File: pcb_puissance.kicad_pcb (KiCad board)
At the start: 2 copper layers, 133.1 x 126.4 mm, 29 parts, among them J1 1755736, J2 1755736, J3 1755736, J4 1755736, J5 1755736, J6 1755736, J7 1755736, J8 1755736, K1 SRD-05VDC-SL-C

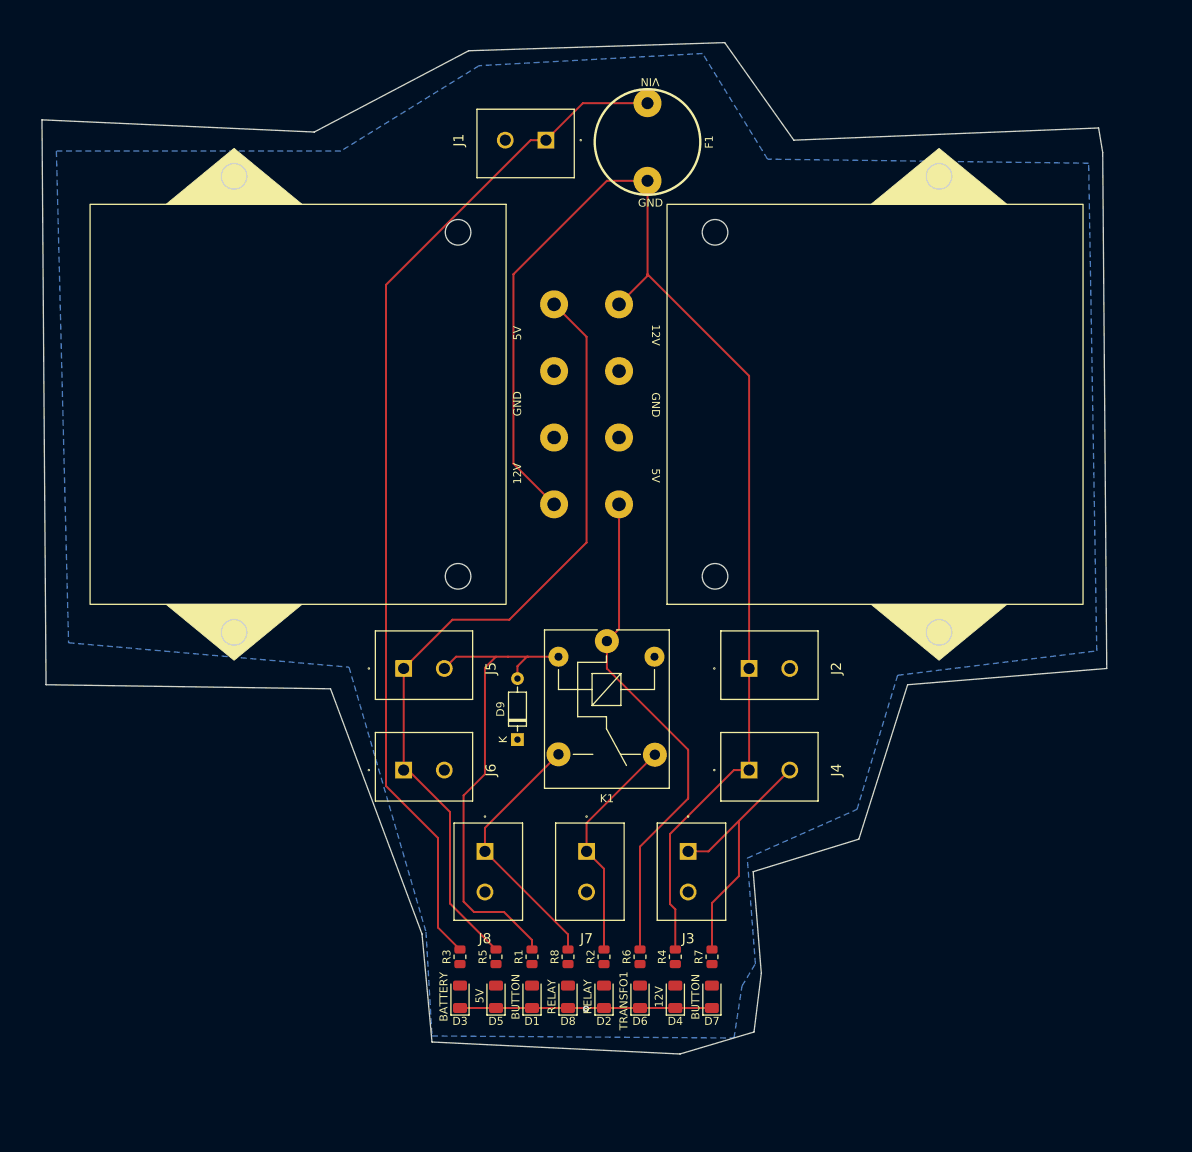
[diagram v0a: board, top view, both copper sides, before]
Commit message: Fin routage + contour/plan de masse/entretoises propres.
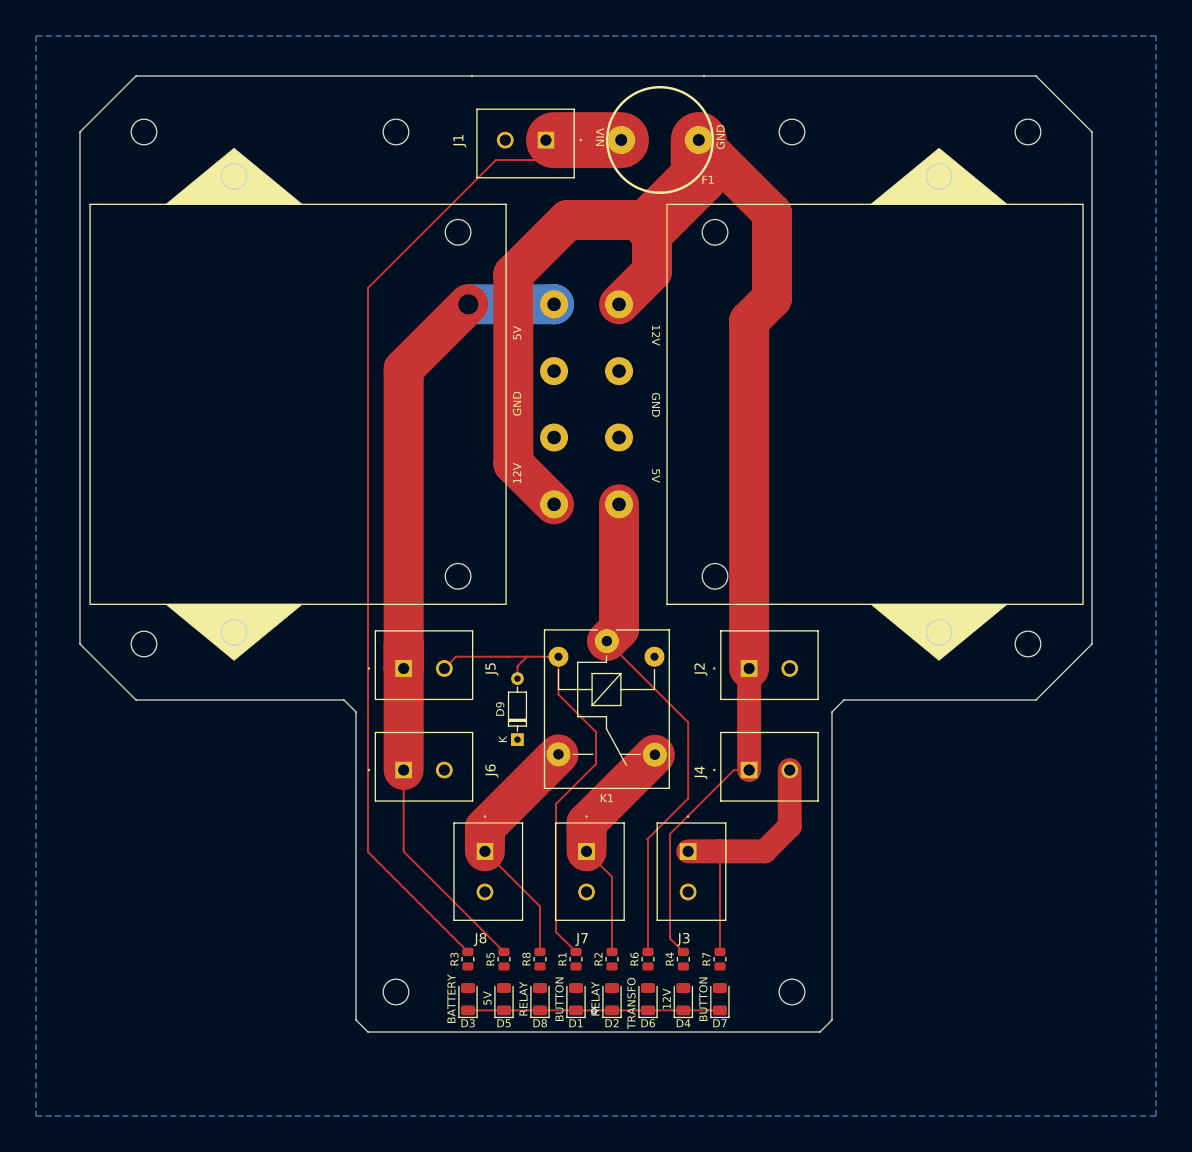
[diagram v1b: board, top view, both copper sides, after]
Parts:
- moved D1 5.51 mm to (82.5, 140.4)
- moved R1 5.51 mm to (82.5, 135.4)
- moved D8 3.51 mm to (78.0, 140.4)
- moved R8 3.51 mm to (78.0, 135.4)
- moved F1 1.58 mm to (93.0, 33.0), turned to 90 degrees
- moved D2 1.04 mm to (87.0, 140.4)
- moved D3 1.04 mm to (69.0, 140.4)
- moved D4 1.04 mm to (95.9, 140.4)
- moved D5 1.04 mm to (73.5, 140.4)
- moved D6 1.04 mm to (91.5, 140.4)
- moved D7 1.04 mm to (100.5, 140.4)
- moved R2 1.04 mm to (87.0, 135.4)
- moved R3 1.04 mm to (69.0, 135.4)
- moved R4 1.04 mm to (95.9, 135.4)
- moved R5 1.04 mm to (73.5, 135.4)
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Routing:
- net +12V: track 164.5 -> 192.6 mm
- net +5V: track 101.1 -> 103.3 mm, vias 0 -> 1
- net BUTTON_NO: track 62.3 -> 60.2 mm
- net BATTERY: track 129.0 -> 131.0 mm
- net RELAY_NC: track 32.5 -> 31.4 mm
- net BUTTON_NC: track 34.4 -> 33.6 mm
- net RELAY_NO: track 28.8 -> 29.5 mm
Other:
- board size 133.1 x 126.4 mm -> 126.5 x 119.5 mm

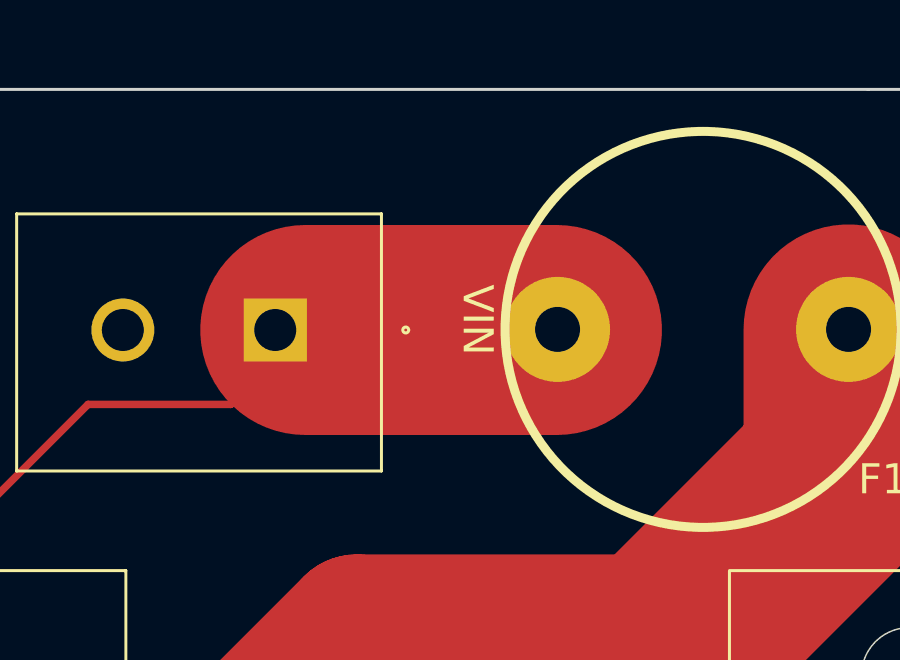
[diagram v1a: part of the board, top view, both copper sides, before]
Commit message: Agrandissement piste batterie -> 10mm
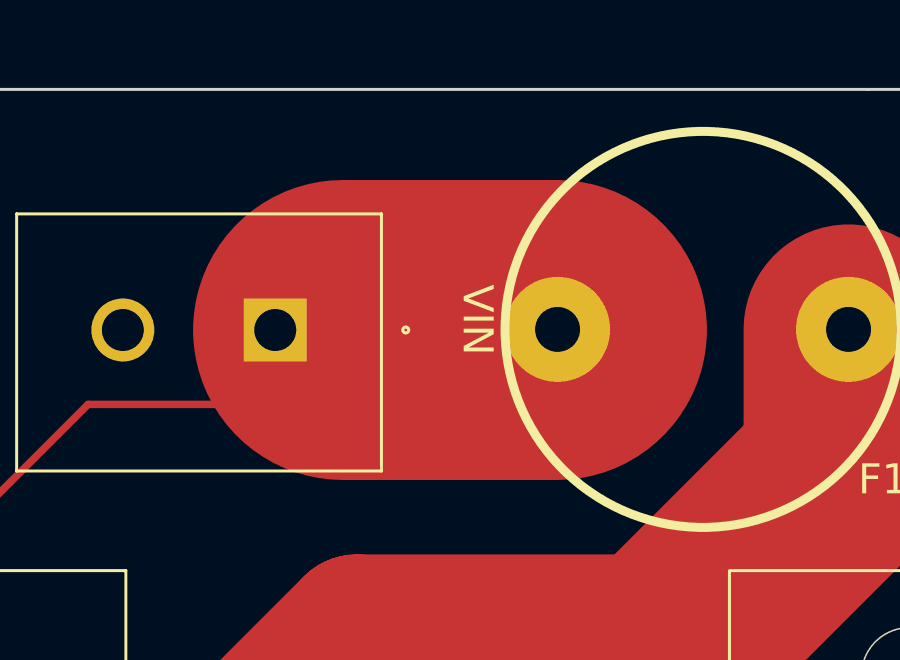
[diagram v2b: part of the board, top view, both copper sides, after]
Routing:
- net BATTERY: track 131.0 -> 127.8 mm
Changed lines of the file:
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@@
   (segment (start 56.5 121.9955) (end 56.5 51.5) (width 0.25) (layer "F.Cu") (net 13))
   (segment (start 88.15 31.65) (end 88.15 33) (width 0.25) (layer "F.Cu") (net 13))
-  (segment (start 79.74 33.02) (end 88.13 33.02) (width 7) (layer "F.Cu") (net 13))
-  (segment (start 76.836897 33.02) (end 78.74 33.02) (width 0.25) (layer "F.Cu") (net 13))
+  (segment (start 81 33.02) (end 88.13 33.02) (width 10) (layer "F.Cu") (net 13))
   (segment (start 56.5 51.5) (end 72.5 35.5) (width 0.25) (layer "F.Cu") (net 13))
   (segment (start 77.26 35.5) (end 79.74 33.02) (width 0.25) (layer "F.Cu") (net 13))

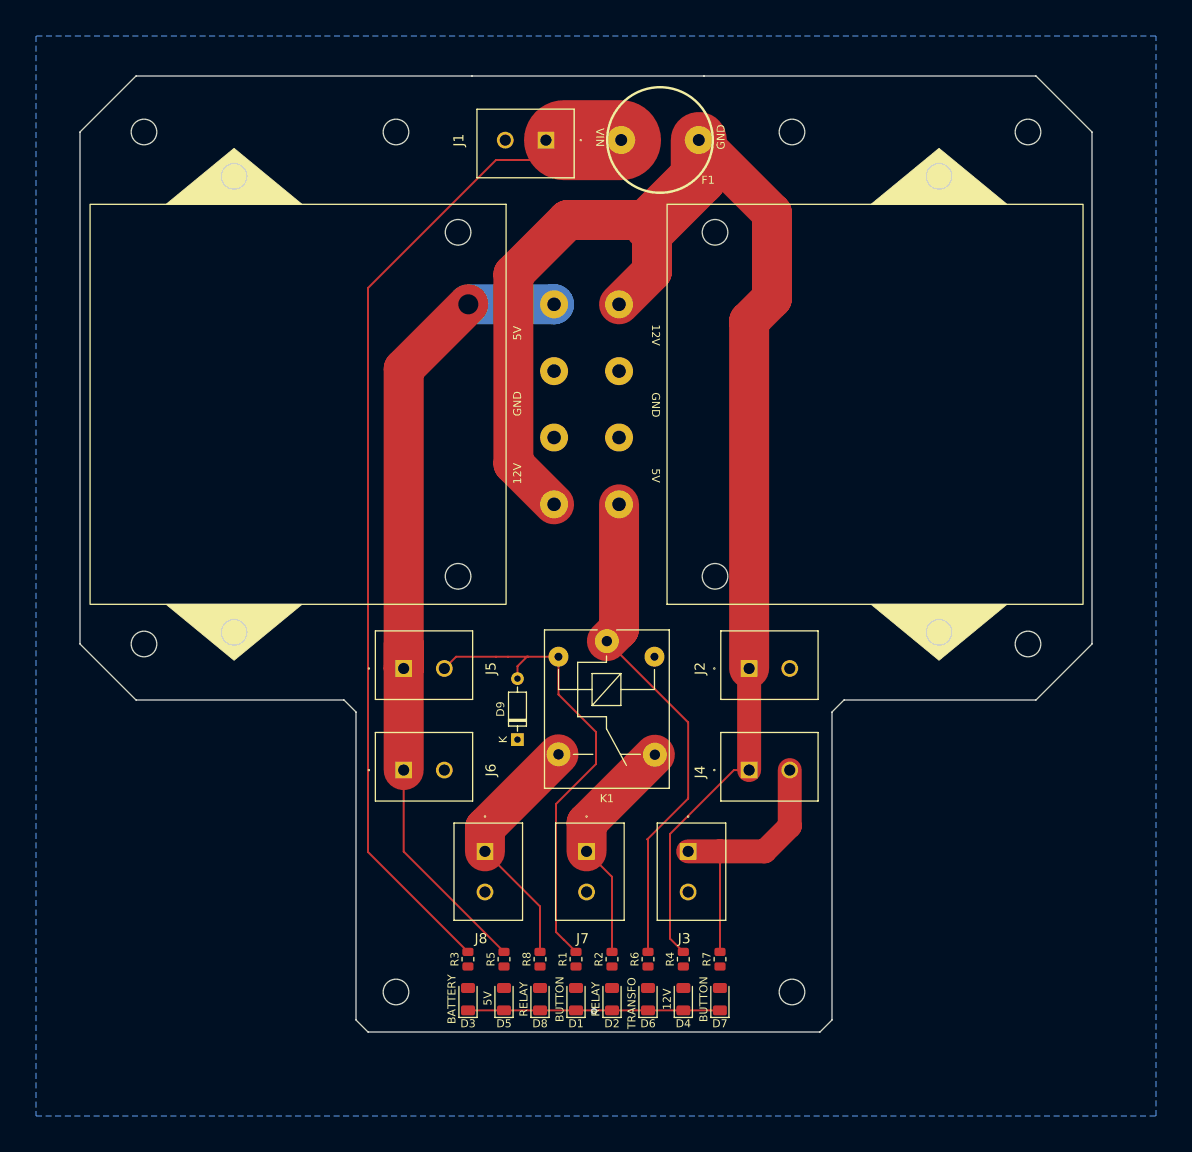
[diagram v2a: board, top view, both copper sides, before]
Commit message: Deplacement connecteurs, petites pistes 0.5mm, ajout connecteurs Dupond, plan de masse Front, pastilles pour les fixations
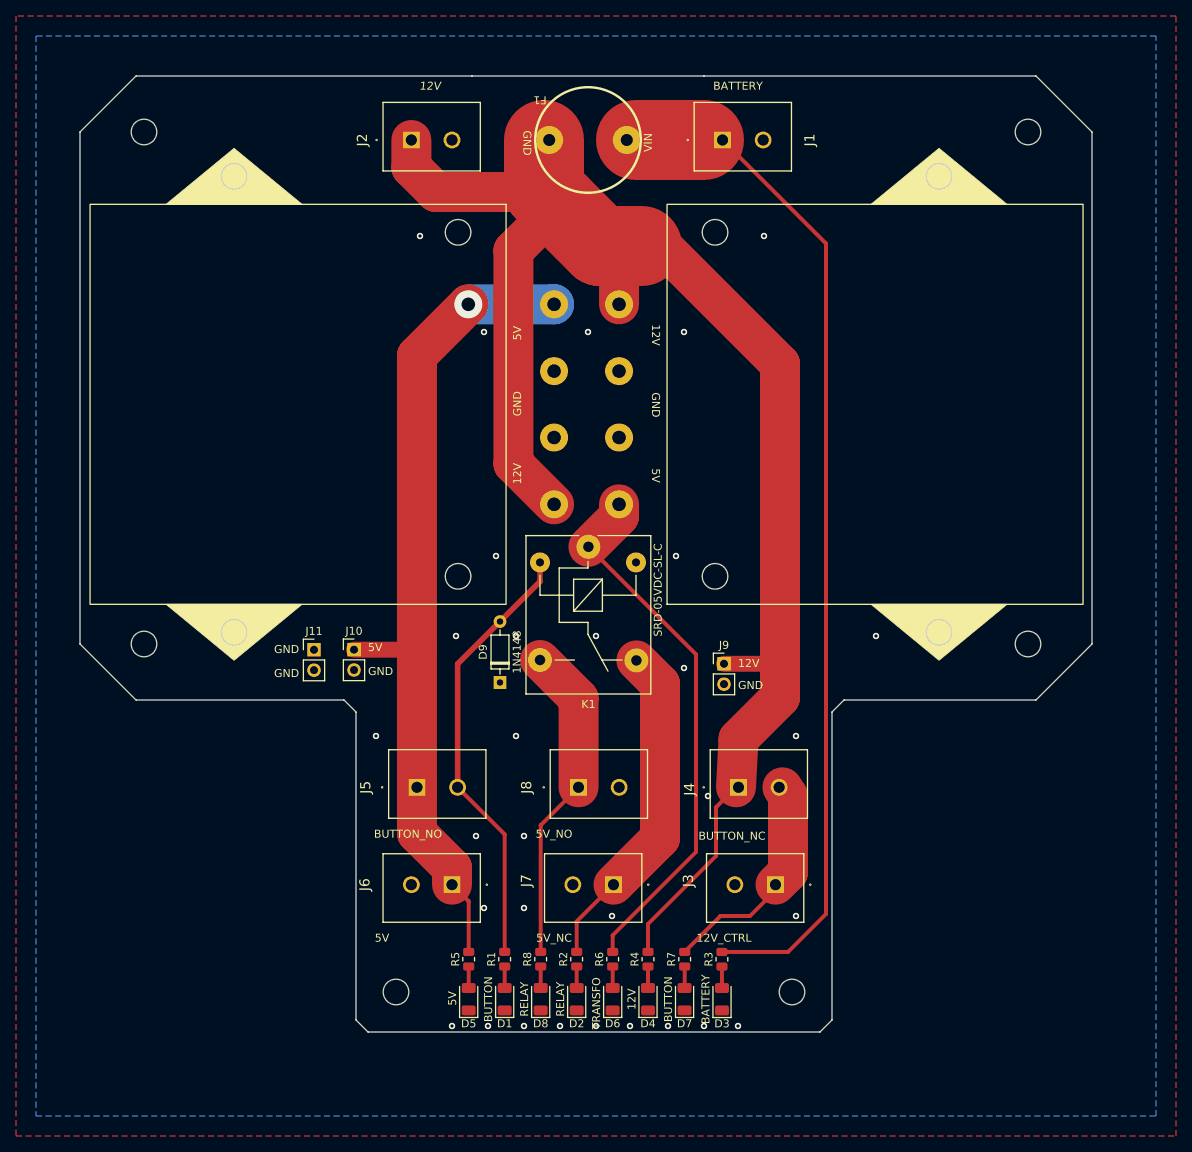
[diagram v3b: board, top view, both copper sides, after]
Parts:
- added J10: Conn_01x02, Connector_PinHeader_2.54mm:PinHeader_1x02_P2.54mm_Vertical, F.Cu at (54.8, 96.7)
- added J11: Conn_01x02, Connector_PinHeader_2.54mm:PinHeader_1x02_P2.54mm_Vertical, F.Cu at (49.8, 96.7)
- added J9: Conn_01x02, Connector_PinHeader_2.54mm:PinHeader_1x02_P2.54mm_Vertical, F.Cu at (101.0, 98.5)
- moved J2 78.4 mm to (61.9, 33.0)
- moved D3 31.8 mm to (100.8, 140.4)
- moved R3 31.8 mm to (100.7, 135.4)
- moved J1 22.1 mm to (100.8, 33.0), turned to 0 degrees
- moved J6 15.5 mm to (67.0, 126.1), turned to 180 degrees
- moved J5 14.9 mm to (62.6, 113.9)
- moved J8 14.2 mm to (82.8, 113.9), turned to 0 degrees
- moved K1 12.0 mm to (84.0, 83.8)
- moved J3 11.7 mm to (107.4, 126.1), turned to 180 degrees
- moved F1 9.00 mm to (84.0, 33.0), turned to -90 degrees
- moved D1 8.92 mm to (73.6, 140.4)
- moved R1 8.92 mm to (73.6, 135.4)
- moved D9 7.47 mm to (73.0, 100.8)
- moved J7 5.35 mm to (87.2, 126.1), turned to 180 degrees
- moved D2 4.42 mm to (82.6, 140.4)
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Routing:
- net GND: track 31.6 -> 0.01 mm, vias 1 -> 31
- net RELAY_NO: track 29.5 -> 42.0 mm
- net +12V: track 192.6 -> 203.4 mm
- net RELAY_NC: track 31.4 -> 40.4 mm
- net BUTTON_NC: track 33.6 -> 28.3 mm
- net BUTTON_NO: track 60.2 -> 55.4 mm
- net TRANSFO1: track 62.9 -> 67.4 mm
- net Net-(D7-A): track 0.00 -> 2.69 mm
- net Net-(D8-A): track 0.00 -> 2.69 mm
- net Net-(D6-A): track 0.00 -> 2.69 mm
- net Net-(D5-A): track 0.00 -> 2.69 mm
- net Net-(D4-A): track 0.00 -> 2.69 mm
- net Net-(D2-A): track 0.00 -> 2.69 mm
- net Net-(D1-A): track 0.00 -> 2.69 mm
- net Net-(D3-A): track 0.00 -> 2.68 mm
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- added copper zone on F.Cu, net GND
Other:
- outline, holes or cut-outs redrawn
- board text added: "12V"
- board text added: "5V"
- board text added: "GND"

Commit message: Pastilles oubliées + ajout vias + plus d'espace pour les connecteurs
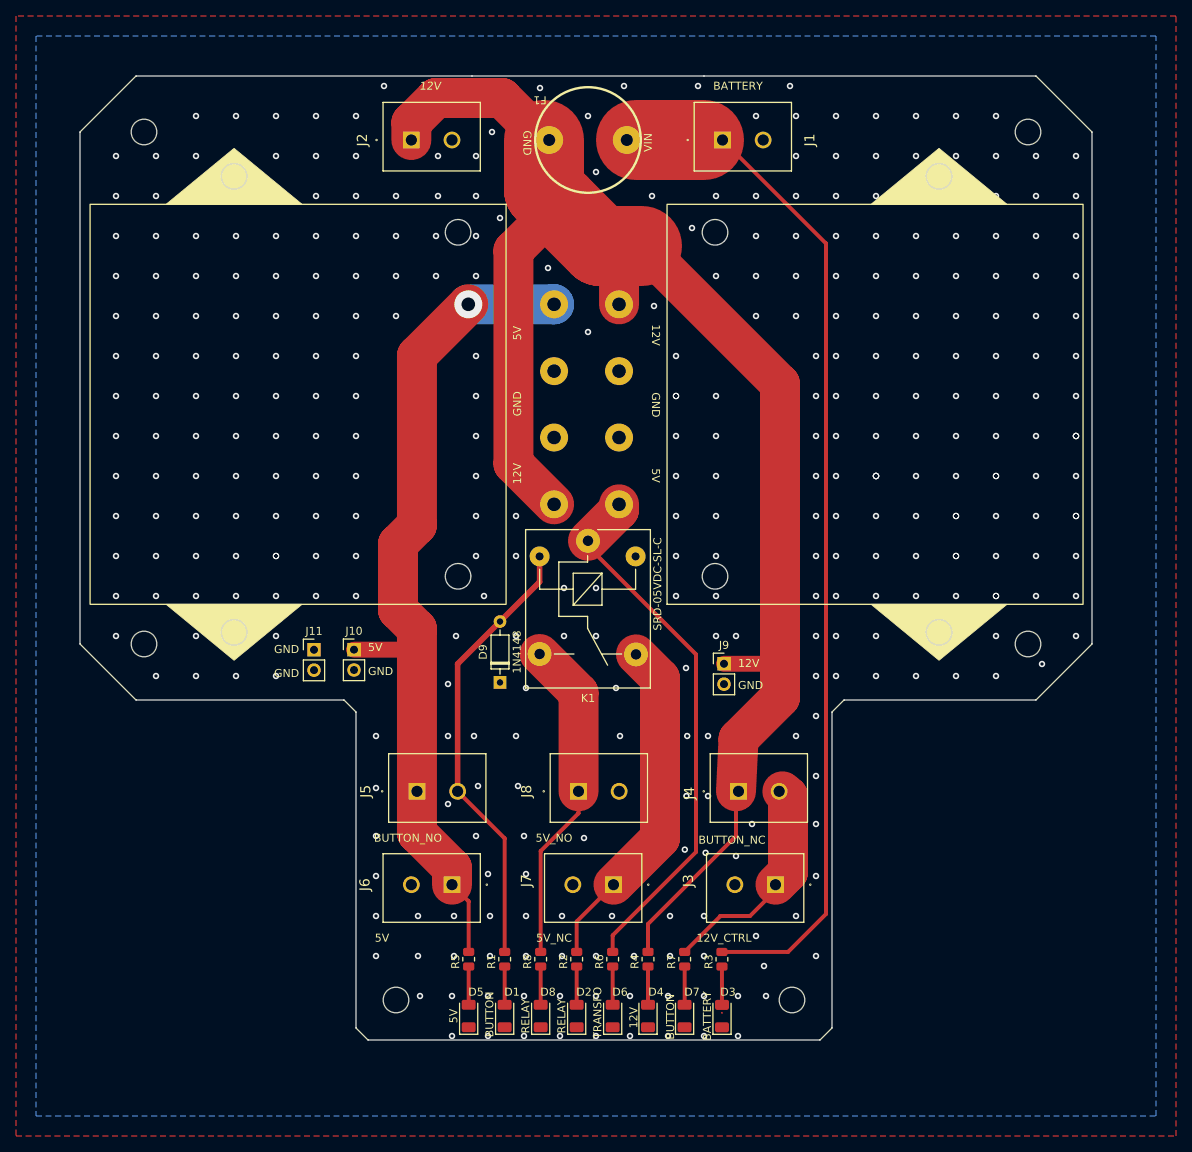
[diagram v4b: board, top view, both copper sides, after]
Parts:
- moved D3 2.10 mm to (100.8, 142.5)
- moved D1 2.10 mm to (73.6, 142.5)
- moved D2 2.10 mm to (82.6, 142.5)
- moved D4 2.10 mm to (91.5, 142.5)
- moved D5 2.10 mm to (69.1, 142.5)
- moved D6 2.10 mm to (87.1, 142.5)
- moved D7 2.10 mm to (96.1, 142.5)
- moved D8 2.10 mm to (78.1, 142.5)
- moved K1 0.75 mm to (84.0, 83.1)
- moved J4 0.50 mm to (102.8, 114.4)
- moved J5 0.50 mm to (62.6, 114.4)
- moved J8 0.50 mm to (82.8, 114.4)
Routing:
- net +12V: track 203.4 -> 207.9 mm
- net Net-(D3-A): track 2.68 -> 4.79 mm
- net Net-(D8-A): track 2.69 -> 4.79 mm
- net Net-(D7-A): track 2.69 -> 4.79 mm
- net Net-(D6-A): track 2.69 -> 4.79 mm
- net Net-(D5-A): track 2.69 -> 4.79 mm
- net Net-(D4-A): track 2.69 -> 4.79 mm
- net Net-(D2-A): track 2.69 -> 4.79 mm
- net Net-(D1-A): track 2.69 -> 4.79 mm
- net +5V: track 104.9 -> 106.9 mm
- net RELAY_NO: track 42.0 -> 42.7 mm
- net RELAY_NC: track 40.4 -> 41.2 mm
- net BUTTON_NO: track 55.4 -> 56.1 mm
- net GND: vias 31 -> 361
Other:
- board size 126.5 x 119.5 mm -> 126.5 x 120.5 mm
